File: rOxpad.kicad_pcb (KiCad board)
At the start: 2 copper layers, 68.3 x 65.1 mm, 25 parts, among them SW1 SW_Push, U1 ATmega16U2-A, U2 PRTR5V0U2X, Y1 16MHz

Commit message: Main board wiring finished (i hope)
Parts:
- moved D1 0.79 mm to (96.8, 88.9)
- moved D2 0.79 mm to (115.9, 88.9)
- moved D3 0.79 mm to (134.9, 88.9)
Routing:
- net +5V: track 90.5 -> 101.8 mm
- net GND: track 168.4 -> 166.9 mm

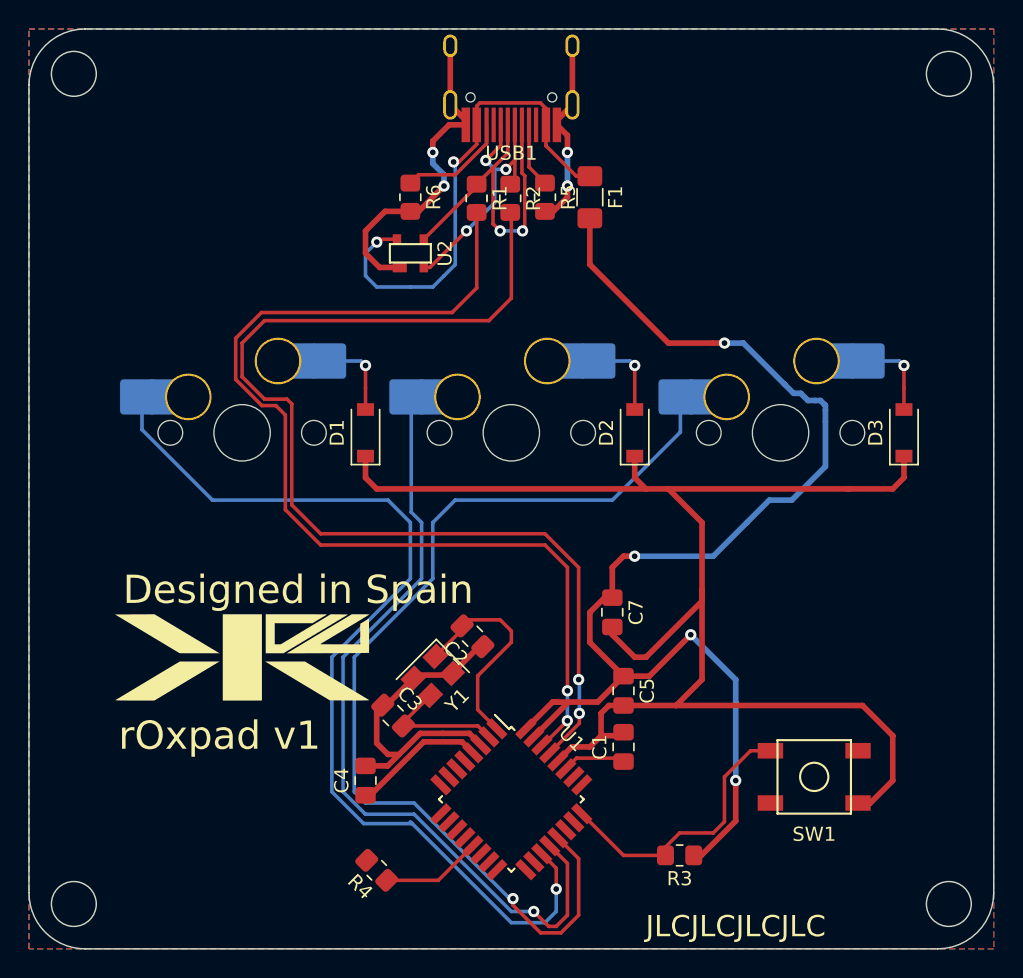
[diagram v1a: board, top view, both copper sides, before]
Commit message: Finished all component markings
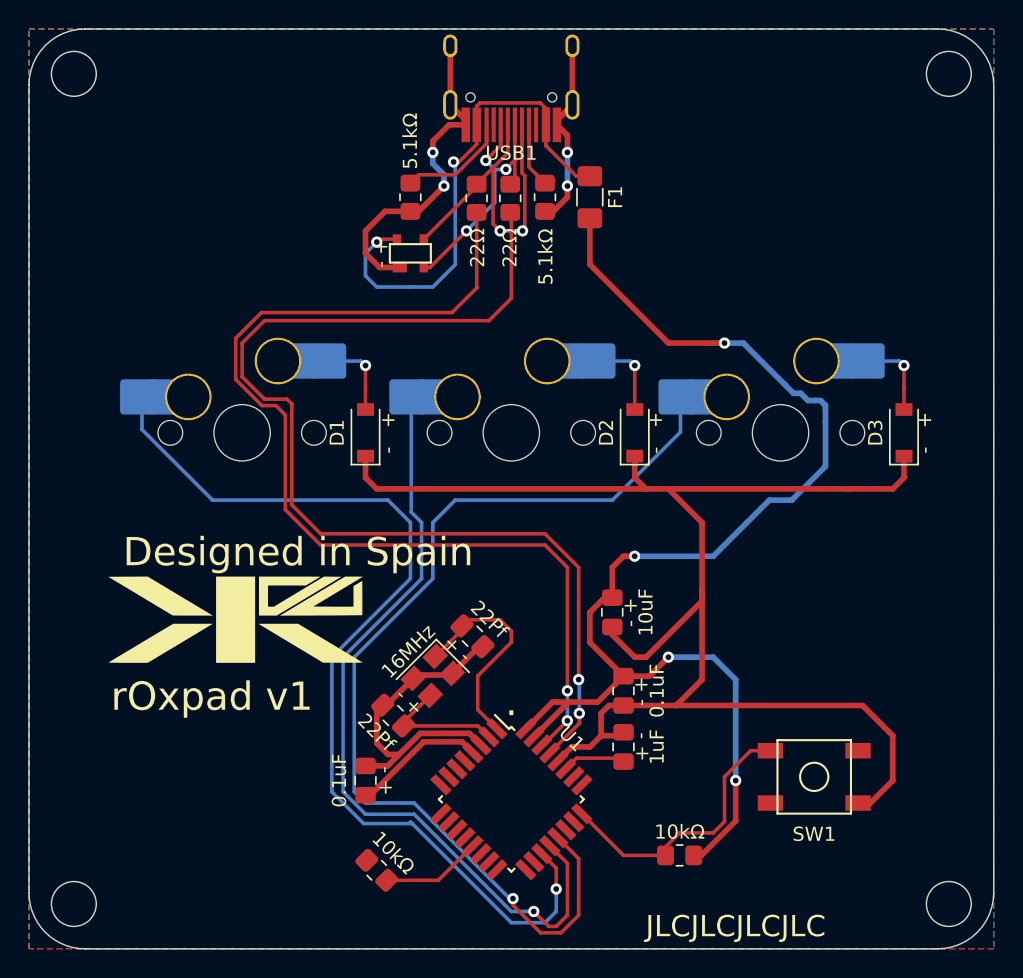
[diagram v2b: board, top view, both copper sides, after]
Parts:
- F1: value Polyfuse_Small -> Polyfuse
- R1, R2: value 22 -> 22Ω
- R3, R4: value 10k -> 10kΩ
- R5, R6: value 5.1k -> 5.1kΩ
- moved G*** 2.71 mm to (87.6, 102.1)
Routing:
- net +5V: track 101.8 -> 100.5 mm
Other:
- board text added: "- +"
- board text added: "."

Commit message: finishing touches
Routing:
- net +5V: track 100.5 -> 105.5 mm
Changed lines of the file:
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@@
   )
   (segment (start 103.657639 110.766953) (end 104.433889 111.543203) (width 0.4) (layer "F.Cu") (net 1))
-  (segment (start 110.077702 107.95) (end 110.33125 107.95) (width 0.4) (layer "F.Cu") (net 1))
   (segment (start 111.209073 107.95) (end 113.2625 107.95) (width 0.4) (layer "F.Cu") (net 1))
   (segment (start 120.0625 118.8) (end 120.601541 118.8) (width 0.4) (layer "F.Cu") (net 1))
   (segment (start 97.179778 114.54375) (end 100.956575 110.766953) (width 0.4) (layer "F.Cu") (net 1))
-  (segment (start 108.181555 109.846147) (end 110.077702 107.95) (width 0.4) (layer "F.Cu") (net 1))
   (segment (start 96.8375 114.54375) (end 97.179778 114.54375) (width 0.4) (layer "F.Cu") (net 1))
   (segment (start 100.956575 110.766953) (end 103.657639 110.766953) (width 0.4) (layer "F.Cu") (net 1))
   (segment (start 116.925 106.11875) (end 118.26875 104.775) (width 0.4) (layer "F.Cu") (net 1))
   (segment (start 112.7125 76.99375) (end 118.26875 82.55) (width 0.4) (layer "F.Cu") (net 1))
+  (segment (start 105.028344 112.137658) (end 105.890044 112.137658) (width 0.4) (layer "F.Cu") (net 1))
   (segment (start 113.75 100.5625) (end 114.3 100.5625) (width 0.4) (layer "F.Cu") (net 1))
   (segment (start 114.3 98.425) (end 114.3 100.5625) (width 0.4) (layer "F.Cu") (net 1))
+  (segment (start 108.181555 109.846147) (end 110.077702 107.95) (width 0.4) (layer "F.Cu") (net 1))
   (segment (start 112.7125 73.71875) (end 112.7125 76.99375) (width 0.4) (layer "F.Cu") (net 1))
   (segment (start 118.26875 82.55) (end 121.349625 82.55) (width 0.4) (layer "F.Cu") (net 1))
@@
   (segment (start 112.7125 101.6) (end 113.75 100.5625) (width 0.4) (layer "F.Cu") (net 1))
   (segment (start 115.09375 106.11875) (end 112.7125 103.7375) (width 0.4) (layer "F.Cu") (net 1))
+  (segment (start 113.2625 107.95) (end 115.09375 106.11875) (width 0.4) (layer "F.Cu") (net 1))
   (segment (start 110.33125 107.95) (end 110.336197 107.954947) (width 0.4) (layer "F.Cu") (net 1))
-  (segment (start 113.2625 107.95) (end 115.09375 106.11875) (width 0.4) (layer "F.Cu") (net 1))
   (segment (start 112.7125 103.7375) (end 112.7125 101.6) (width 0.4) (layer "F.Cu") (net 1))
   (segment (start 115.09375 97.63125) (end 114.3 98.425) (width 0.4) (layer "F.Cu") (net 1))
+  (segment (start 104.433889 111.543203) (end 105.028344 112.137658) (width 0.4) (layer "F.Cu") (net 1))
+  (segment (start 110.336197 107.954947) (end 111.209073 107.954947) (width 0.4) (layer "F.Cu") (net 1))
+  (segment (start 105.890044 112.137658) (end 108.181555 109.846147) (width 0.4) (layer "F.Cu") (net 1))
   (segment (start 120.601541 118.8) (end 123.03125 116.370291) (width 0.4) (layer "F.Cu") (net 1))
   (segment (start 115.09375 106.11875) (end 116.91925 106.11875) (width 0.4) (layer "F.Cu") (net 1))
   (segment (start 116.91925 106.11875) (end 116.925 106.11875) (width 0.4) (layer "F.Cu") (net 1))
   (segment (start 122.2375 82.55) (end 121.44375 82.55) (width 0.4) (layer "F.Cu") (net 1))
-  (segment (start 110.336197 107.954947) (end 111.125 107.954947) (width 0.4) (layer "F.Cu") (net 1))
+  (segment (start 110.077702 107.95) (end 110.33125 107.95) (width 0.4) (layer "F.Cu") (net 1))
   (segment (start 108.74724 110.411833) (end 111.209073 107.95) (width 0.4) (layer "F.Cu") (net 1))
   (segment (start 115.88175 97.63125) (end 115.09375 97.63125) (width 0.4) (layer "F.Cu") (net 1))
@@
   (segment (start 93.6625 96.8375) (end 91.167 94.342) (width 0.254) (layer "F.Cu") (net 9))
   (segment (start 102.96525 80.391) (end 104.70825 78.648) (width 0.254) (layer "F.Cu") (net 9))
-  (segment (start 109.312926 110.977518) (end 109.416732 110.977518) (width 0.254) (layer "F.Cu") (net 9))
   (segment (start 111.124862 107.154947) (end 111.125 107.154809) (width 0.254) (layer "F.Cu") (net 9))
   (segment (start 111.125 98.425) (end 109.5375 96.8375) (width 0.254) (layer "F.Cu") (net 9))
@@
   (segment (start 105.979339 70.260589) (end 105.348786 69.630036) (width 0.254) (layer "B.Cu") (net 10))
   (segment (start 106.773088 70.260589) (end 105.979339 70.260589) (width 0.254) (layer "B.Cu") (net 10))
-  (segment (start 109.878611 111.543203) (end 111.969457 109.452357) (width 0.254) (layer "F.Cu") (net 11))
   (segment (start 111.969457 109.452357) (end 111.969457 108.7495) (width 0.254) (layer "F.Cu") (net 11))
   (segment (start 88.10625 82.55) (end 88.10625 84.93125) (width 0.254) (layer "F.Cu") (net 11))
   (segment (start 93.6625 96.04375) (end 109.5375 96.04375) (width 0.254) (layer "F.Cu") (net 11))
-  (segment (start 109.878611 111.543203) (end 109.879319 111.543203) (width 0.254) (layer "F.Cu") (net 11))
+  (segment (start 109.878611 111.543203) (end 111.969457 109.452357) (width 0.254) (layer "F.Cu") (net 11))
   (segment (start 107.15625 73.383717) (end 107.15625 79.375) (width 0.254) (layer "F.Cu") (net 11))
   (segment (start 88.10625 84.93125) (end 89.69375 86.51875) (width 0.254) (layer "F.Cu") (net 11))
@@
   (segment (start 110.33125 121.18125) (end 110.33125 119.703306) (width 0.254) (layer "F.Cu") (net 24))
   (via (at 110.33125 121.18125) (size 0.8) (drill 0.4) (layers "F.Cu" "B.Cu") (net 24))
-  (segment (start 100.0125 116.41875) (end 100.14375 116.55) (width 0.254) (layer "B.Cu") (net 24))
   (segment (start 100.14375 116.55) (end 96.70625 116.55) (width 0.254) (layer "B.Cu") (net 24))
   (segment (start 107.15625 123.5625) (end 109.5375 123.5625) (width 0.254) (layer "B.Cu") (net 24))
@@
   (segment (start 98.338357 120.563357) (end 101.989829 120.563357) (width 0.254) (layer "F.Cu") (net 27))
   (segment (start 101.989829 120.563357) (end 104.433889 118.119297) (width 0.254) (layer "F.Cu") (net 27))
-  (segment (start 104.433889 118.119297) (end 104.433889 118.347361) (width 0.254) (layer "F.Cu") (net 27))
   (segment (start 108.40625 70.1) (end 108.40625 67.11) (width 0.254) (layer "F.Cu") (net 28))
   (segment (start 109.5375 71.23125) (end 108.40625 70.1) (width 0.254) (layer "F.Cu") (net 28))
